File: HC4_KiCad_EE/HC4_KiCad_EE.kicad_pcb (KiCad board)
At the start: 2 copper layers, 150.4 x 175 mm, 168 parts, among them IC1 RAM, IC10 74HC4002, IC11 74HC161, IC12 74HC377, IC13 74HC161, IC14 74HC161, IC15 74HC161, IC16 74HC257, IC17 74HC257, IC18 74HC32, IC19 74HC74, IC2 ROM, IC20 74HC00, IC21 74HC4053, IC22 74HC04, IC23 74HC151, IC24 74HC14, IC3 74HC153, IC4 74HC153, IC5 74HC153, IC6 74HC153, IC7 74HC283, IC8 74HC257, IC9 74HC244, J1 Power, J2 CE, J3 Expantion_Connector, SW1 SW_SPDT, SW2 Bus_Open, SW3 SW_Push, SW4 SW_Push, SW5 SW_SPDT

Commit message: チップ集合抵抗に変更、基板作成開始
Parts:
- removed CP19, CP20, CP21, CP22, CP23, CP24: 0.1u, Capacitor_THT:C_Disc_D3.0mm_W1.6mm_P2.50mm
- removed D10, D11, D12, D13, D14, D15, D16, D17, D18, D19, D2, D20, D21, D22, D23, D24, D25, D26, D27, D28, D29, D3, D30, D31, D32, D33, D34, D35, D36, D37, D38, D39, D4, D40, D41, D5, D6, D7, D8, D9: D, Library:DO-35_horizontal_anodeup_Smallhole
- removed G***: LOGO, LOGO
- removed IC16, IC17: 74HC257, Package_DIP:DIP-16_W7.62mm_Socket
- removed IC18: 74HC32, Package_DIP:DIP-14_W7.62mm_Socket
- removed IC19: 74HC74, Package_DIP:DIP-14_W7.62mm_Socket
- removed IC20: 74HC00, Package_DIP:DIP-14_W7.62mm_Socket
- removed IC21: 74HC4053, Package_DIP:DIP-16_W7.62mm_Socket
- removed IC22: 74HC04, Package_DIP:DIP-14_W7.62mm_Socket
- removed IC23: 74HC151, Package_DIP:DIP-16_W7.62mm_Socket
- removed IC24: 74HC14, Package_DIP:DIP-14_W7.62mm_Socket
- removed JP1: Jumper, Connector_PinHeader_2.54mm:PinHeader_1x03_P2.54mm_Vertical
- removed R10: 100k, Resistor_THT:R_Axial_DIN0207_L6.3mm_D2.5mm_P7.62mm_Horizontal
- removed R11: Socket, Resistor_THT:R_Axial_DIN0207_L6.3mm_D2.5mm_P7.62mm_Horizontal
- removed R12, R15: 100, Resistor_THT:R_Axial_DIN0207_L6.3mm_D2.5mm_P7.62mm_Horizontal
- removed R13, R14: 1k, Resistor_THT:R_Axial_DIN0207_L6.3mm_D2.5mm_P7.62mm_Horizontal
- added C5: 10u, Capacitor_THT:C_Radial_D5.0mm_H5.0mm_P2.00mm, F.Cu at (190.7, 110.7)
- added H1: MountingHole, MountingHole:MountingHole_3.2mm_M3, F.Cu at (141.5, 62.5)
- added H2: MountingHole, MountingHole:MountingHole_3.2mm_M3, F.Cu at (48.5, 62.5)
- added H3: MountingHole, MountingHole:MountingHole_3.2mm_M3, F.Cu at (48.5, 151.5)
- added H4: MountingHole, MountingHole:MountingHole_3.2mm_M3, F.Cu at (141.5, 151.5)
- added J4: AVR-UPDI-6, Connector_PinHeader_2.54mm:PinHeader_2x03_P2.54mm_Vertical, F.Cu at (260.4, 90.8)
- added LD42: Chip, LED_SMD:LED_0603_1608Metric, F.Cu at (254.1, 66.3)
- added LD43: Chip, LED_SMD:LED_0603_1608Metric, F.Cu at (254.1, 68.9)
- added LD44: CLK, LED_THT:LED_D5.0mm, F.Cu at (180.3, 107.1)
- added LD45: RESET, LED_THT:LED_D5.0mm, F.Cu at (180.3, 114.5)
- added LD46: Chip, LED_SMD:LED_0603_1608Metric, F.Cu at (268.1, 69.5)
- added LD47: Chip, LED_SMD:LED_0603_1608Metric, F.Cu at (268.1, 72.1)
- added LD48: Chip, LED_SMD:LED_0603_1608Metric, F.Cu at (268.1, 74.7)
- added LD49: Chip, LED_SMD:LED_0603_1608Metric, F.Cu at (268.1, 77.2)
- added RN10: 1k, Resistor_SMD:R_Array_Convex_4x0603, F.Cu at (255.0, 116.8)
- added RN11: 1k, Resistor_SMD:R_Array_Convex_4x0603, F.Cu at (246.1, 57.4)
- added RN12: 1k, Resistor_SMD:R_Array_Convex_4x0603, F.Cu at (250.2, 57.4)
- added RN13: 1k, Resistor_SMD:R_Array_Convex_4x0603, F.Cu at (254.4, 57.4)
- added RN14: 1k, Resistor_SMD:R_Array_Convex_4x0603, F.Cu at (197.0, 109.8)
- added RN15: 1k, Resistor_SMD:R_Array_Convex_4x0603, F.Cu at (272.1, 70.6)
- added RN9: 1k, Resistor_SMD:R_Array_Convex_4x0603, F.Cu at (250.8, 116.8)
- added U1: ATmega4809-A, Package_QFP:TQFP-48_7x7mm_P0.5mm, F.Cu at (67.9, 146.7)
- added U2: CH340E, Package_SO:MSOP-10_3x3mm_P0.5mm, F.Cu at (57.8, 141.6)
- C2: value 10u -> 0.1u; footprint Capacitor_THT:CP_Radial_D5.0mm_P2.50mm -> Capacitor_SMD:C_0603_1608Metric
- C4: value 10u(Socket) -> 10u; footprint Capacitor_THT:C_Radial_D5.0mm_H5.0mm_P2.00mm -> Capacitor_THT:CP_Radial_D5.0mm_P2.50mm
- CP1, CP10, CP11, CP12, CP13, CP14, CP15, CP16, CP17, CP18, CP2, CP3, CP4, CP5, CP6, CP7, CP8, CP9: footprint Capacitor_THT:C_Disc_D3.0mm_W1.6mm_P2.50mm -> Capacitor_SMD:C_0603_1608Metric
- D1: value 5.6V -> C-551SRD; footprint Diode_THT:D_DO-34_SOD68_P7.62mm_Horizontal -> Display_7Segment:D1X8K
- F1: value Polyfuse -> 500mA
- IC1: value RAM -> 74HC86; footprint Package_DIP:DIP-28_W15.24mm -> Package_SO:SO-14_5.3x10.2mm_P1.27mm
- IC10: value 74HC4002 -> 74HC161; footprint Package_DIP:DIP-14_W7.62mm_Socket -> Package_SO:SO-16_5.3x10.2mm_P1.27mm
- IC11: value 74HC161 -> 74HC02; footprint Package_DIP:DIP-16_W7.62mm_Socket -> Package_SO:SO-14_5.3x10.2mm_P1.27mm
- IC12: value 74HC377 -> 74HC00; footprint Package_DIP:DIP-20_W7.62mm_Socket -> Package_SO:SO-14_5.3x10.2mm_P1.27mm
- IC13: value 74HC161 -> 74HC4053; footprint Package_DIP:DIP-16_W7.62mm_Socket -> Package_SO:SO-16_5.3x10.2mm_P1.27mm
- IC14: value 74HC161 -> 74HC74; footprint Package_DIP:DIP-16_W7.62mm_Socket -> Package_SO:SO-14_5.3x10.2mm_P1.27mm
- IC15: value 74HC161 -> 74HC14; footprint Package_DIP:DIP-16_W7.62mm_Socket -> Package_SO:SO-14_5.3x10.2mm_P1.27mm
- IC2: value ROM -> 74HC283; footprint Package_DIP:DIP-28_W15.24mm -> Package_SO:SO-16_5.3x10.2mm_P1.27mm
- IC3, IC4: value 74HC153 -> 74HC253; footprint Package_DIP:DIP-16_W7.62mm_Socket -> Package_SO:SO-16_5.3x10.2mm_P1.27mm
- IC5: value 74HC153 -> 74HC244; footprint Package_DIP:DIP-16_W7.62mm_Socket -> Package_SO:TSSOP-20_4.4x6.5mm_P0.65mm
- IC6: value 74HC153 -> 74HC377; footprint Package_DIP:DIP-16_W7.62mm_Socket -> Package_SO:TSSOP-20_4.4x6.5mm_P0.65mm
- IC7: value 74HC283 -> 4511; footprint Package_DIP:DIP-16_W7.62mm_Socket -> Package_SO:SO-16_5.3x10.2mm_P1.27mm
- IC8: value 74HC257 -> 74HC377; footprint Package_DIP:DIP-16_W7.62mm_Socket -> Package_SO:TSSOP-20_4.4x6.5mm_P0.65mm
- IC9: value 74HC244 -> 74HC161; footprint Package_DIP:DIP-20_W7.62mm_Socket -> Package_SO:SO-16_5.3x10.2mm_P1.27mm
- J1: value Power -> USB_B_Mini; footprint Connector_BarrelJack:BarrelJack_GCT_DCJ200-10-A_Horizontal -> Connector_USB:USB_Mini-B_Wuerth_65100516121_Horizontal
- J2: value CE -> Port_IN; footprint Connector_PinSocket_2.54mm:PinSocket_1x01_P2.54mm_Vertical -> Connector_PinHeader_2.54mm:PinHeader_1x04_P2.54mm_Vertical
- J3: value Expantion_Connector -> Port_A; footprint Connector_PinHeader_2.54mm:PinHeader_2x20_P2.54mm_Vertical -> Connector_PinHeader_2.54mm:PinHeader_1x04_P2.54mm_Vertical
- LD2: value LED -> Carry
- LD31: value LED -> ACT; footprint LED_THT:LED_Rectangular_W5.0mm_H2.0mm -> LED_SMD:LED_0603_1608Metric
- LD32, LD33, LD34, LD35, LD36, LD37, LD38, LD39: value LED -> Chip; footprint LED_THT:LED_Rectangular_W5.0mm_H2.0mm -> LED_SMD:LED_0603_1608Metric
- LD40, LD41: value D -> Chip; footprint LED_THT:LED_D5.0mm -> LED_SMD:LED_0603_1608Metric
- R1, R2, R3, R4: footprint Resistor_THT:R_Axial_DIN0207_L6.3mm_D2.5mm_P7.62mm_Horizontal -> Resistor_SMD:R_0603_1608Metric
- R5: value 10k -> 100k; footprint Resistor_THT:R_Axial_DIN0207_L6.3mm_D2.5mm_P7.62mm_Horizontal -> Resistor_SMD:R_0603_1608Metric
- R6: value 10k -> 33k; footprint Resistor_THT:R_Axial_DIN0207_L6.3mm_D2.5mm_P7.62mm_Horizontal -> Resistor_SMD:R_0603_1608Metric
- R7: value 1k -> 3.3k; footprint Resistor_THT:R_Axial_DIN0207_L6.3mm_D2.5mm_P7.62mm_Horizontal -> Resistor_SMD:R_0603_1608Metric
- R8: value 1k -> 100; footprint Resistor_THT:R_Axial_DIN0207_L6.3mm_D2.5mm_P7.62mm_Horizontal -> Resistor_SMD:R_0603_1608Metric
- R9: value 10k -> 100; footprint Resistor_THT:R_Axial_DIN0207_L6.3mm_D2.5mm_P7.62mm_Horizontal -> Resistor_SMD:R_0603_1608Metric
- RN1, RN2, RN5: footprint Resistor_THT:R_Array_SIP5 -> Resistor_SMD:R_Array_Convex_4x0603
- RN3: value R_Network04_Split -> 1k; footprint Resistor_THT:R_Array_SIP5 -> Resistor_SMD:R_Array_Convex_4x0603
- RN4: value R_Network08_Split -> 1k; footprint Resistor_THT:R_Array_SIP9 -> Resistor_SMD:R_Array_Convex_4x0603
- RN6, RN7: footprint Resistor_THT:R_Array_SIP9 -> Resistor_SMD:R_Array_Convex_4x0603
- RN8: value 10k -> 1k; footprint Resistor_THT:R_Array_SIP9 -> Resistor_SMD:R_Array_Convex_4x0603
- SW1: value SW_SPDT -> SW_DIP_x04; footprint Button_Switch_THT:SW_Slide-03_Wuerth-WS-SLTV_10x2.5x6.4_P2.54mm -> Button_Switch_THT:SW_DIP_SPSTx04_Slide_9.78x12.34mm_W7.62mm_P2.54mm
- SW2: value Bus_Open -> SW_Push; footprint Button_Switch_THT:SW_Slide-03_Wuerth-WS-SLTV_10x2.5x6.4_P2.54mm -> Button_Switch_THT:SW_PUSH_6mm
- SW4: value SW_Push -> FreqSel; footprint Button_Switch_THT:SW_PUSH_6mm -> Button_Switch_THT:SW_Slide-03_Wuerth-WS-SLTV_10x2.5x6.4_P2.54mm
- moved F1 227.7 mm to (231.9, 56.8)
- moved LD41 224.6 mm to (254.1, 63.7), turned to 0 degrees
- moved LD40 222.7 mm to (254.1, 61.1), turned to 0 degrees
- moved RN7 218.0 mm to (229.5, 119.5)
- moved C1 217.7 mm to (237.5, 70.4), turned to 0 degrees
- moved LD32 214.8 mm to (246.0, 61.1), turned to 0 degrees
- moved LD33 212.7 mm to (246.0, 63.7), turned to 0 degrees
- moved LD34 210.6 mm to (246.0, 66.3), turned to 0 degrees
- moved CP17 210.2 mm to (268.9, 63.9), turned to 0 degrees
- moved LD36 208.8 mm to (250.1, 61.1), turned to 0 degrees
- moved LD35 208.5 mm to (246.0, 68.9), turned to 0 degrees
- moved CP16 208.3 mm to (268.9, 61.3), turned to 0 degrees
- moved C2 207.5 mm to (256.1, 78.4), turned to 0 degrees
- moved LD37 206.6 mm to (250.1, 63.7), turned to 0 degrees
- moved LD38 204.5 mm to (250.1, 66.3), turned to 0 degrees
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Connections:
- C2 pad 1: Net-(C2-Pad1) -> GND
- C2 pad 2: GND -> Net-(U2-V3)
- C4 pad 2: Net-(SW5-A) -> GND
- D1 pad 1: VCC -> Net-(D1-E)
- D1 pad 2: GND -> Net-(D1-D)
- IC1 pad 1: VCC -> /ALU/ALU_in_A0
- IC1 pad 10: /Address BUS/RAM_A0 -> /ALU/ALU_in_B2
- IC1 pad 11: /Data BUS/Stack0 -> /ALU/XOR3
- IC1 pad 12: /Data BUS/Stack1 -> /ALU/ALU_in_A3
- IC1 pad 13: /Data BUS/Stack2 -> /ALU/ALU_in_B3
- IC1 pad 14: GND -> VCC
- IC1 pad 2: VCC -> /ALU/ALU_in_B0
- IC1 pad 3: /Address BUS/RAM_A7 -> /ALU/XOR0
- IC1 pad 4: /Address BUS/RAM_A6 -> /ALU/ALU_in_A1
- IC1 pad 5: /Address BUS/RAM_A5 -> /ALU/ALU_in_B1
- IC1 pad 6: /Address BUS/RAM_A4 -> /ALU/XOR1
- IC1 pad 7: /Address BUS/RAM_A3 -> GND
- IC1 pad 8: /Address BUS/RAM_A2 -> /ALU/XOR2
- IC1 pad 9: /Address BUS/RAM_A1 -> /ALU/ALU_in_A2
- IC10 pad 1: /ALU/I1a -> ~{RESET}
- IC10 pad 10: /Data BUS/Stack2 -> VCC
- IC10 pad 11: /Data BUS/Stack1 -> /Program Counter/PC_3
- IC10 pad 12: /Data BUS/Stack0 -> /Program Counter/PC_2
- IC10 pad 13: /Data BUS/BUS_Zero -> /Program Counter/PC_1
- IC10 pad 14: VCC -> /Program Counter/PC_0
- IC10 pad 2: Net-(D18-K) -> CLK
- IC10 pad 3: Net-(D18-K) -> /ALU/ALU_in_A0
- IC10 pad 4: Net-(D22-K) -> /ALU/ALU_in_A1
- IC10 pad 5: Net-(D22-K) -> /ALU/ALU_in_A2
- IC10 pad 6: (no net) -> /ALU/ALU_in_A3
- IC10 pad 7: GND -> VCC
- IC10 pad 8: (no net) -> GND
- IC10 pad 9: /Data BUS/Stack3 -> /Instruction Decoder/~{JMP}
- IC11 pad 1: ~{RESET} -> /Instruction Decoder/READ
- IC11 pad 10: GND -> /Instruction Decoder/Carry_EN
- IC11 pad 11: /ALU/ALU_in_A3 -> VCC
- IC11 pad 12: /ALU/ALU_in_A2 -> VCC
- IC11 pad 13: /ALU/ALU_in_A1 -> unconnected-(IC11-Pad13)
- IC11 pad 14: /ALU/ALU_in_A0 -> VCC
- IC11 pad 2: CLK -> /ALU/Instruction_6
- IC11 pad 3: /Data BUS/Stack0 -> /ALU/Instruction_5
- IC11 pad 4: /Data BUS/Stack1 -> unconnected-(IC11-Pad4)
- IC11 pad 5: /Data BUS/Stack2 -> VCC
- IC11 pad 6: /Data BUS/Stack3 -> VCC
- IC11 pad 8: GND -> /ALU/Instruction_7
- IC11 pad 9: /Instruction Decoder/~{STACK_LE} -> /ALU/Instruction_6
- IC12 pad 1: /Instruction Decoder/~{STACK_LE} -> /Instruction Decoder/READ
- IC12 pad 10: GND -> /ALU/Instruction_6
- IC12 pad 11: CLK -> /Instruction Decoder/~{STACK_LE}
- IC12 pad 12: /Data BUS/Level_C0 -> /Instruction Decoder/~{Is_JP}
- IC12 pad 13: /ALU/ALU_in_B3 -> /ALU/Instruction_7
- IC12 pad 14: /ALU/ALU_in_B2 -> VCC
- IC12 pad 2: /ALU/ALU_in_B0 -> CLK2
- IC12 pad 3: /ALU/ALU_in_A0 -> /Instruction Decoder/~{RAM_RD}
- IC12 pad 4: /ALU/ALU_in_A1 -> /ALU/Instruction_7
- IC12 pad 5: /ALU/ALU_in_B1 -> CLK2
- IC12 pad 6: /ALU/ALU_in_B2 -> /Instruction Decoder/~{RAM_WR}
- IC12 pad 7: /ALU/ALU_in_A2 -> GND
- IC12 pad 8: /ALU/ALU_in_A3 -> /Instruction Decoder/~{Is_JP}
- IC12 pad 9: /ALU/ALU_in_B3 -> /ALU/Instruction_7
- IC13 pad 1: ~{RESET} -> /Instruction Decoder/Carry_Flg
- IC13 pad 10: Net-(IC13-ENT) -> /ALU/Instruction_1
- IC13 pad 11: /Program Counter/PC_8 -> /Instruction Decoder/Carry_EN
- IC13 pad 12: /Program Counter/PC_9 -> /Instruction Decoder/Carry_Flg
- IC13 pad 13: /Program Counter/PC_10 -> /ALU/Carry_OUT
- IC13 pad 14: /Program Counter/PC_11 -> Net-(IC13-X)
- IC13 pad 15: unconnected-(IC13-CO-Pad15) -> Net-(IC13-Y)
- IC13 pad 2: CLK -> /ALU/Instruction_0
- IC13 pad 3: /Data BUS/Level_C3 -> VCC
- IC13 pad 4: /Data BUS/Level_C2 -> /Instruction Decoder/~{JMP}
- IC13 pad 5: /Data BUS/Level_C1 -> Net-(IC13-Y)
- IC13 pad 6: /Data BUS/Level_C0 -> GND
- IC13 pad 7: VCC -> GND
- IC13 pad 9: /Instruction Decoder/~{JMP} -> /Instruction Decoder/~{Is_JP}
- IC14 pad 10: Net-(IC14-ENT) -> VCC
- IC14 pad 11: /Program Counter/PC_4 -> VCC
- IC14 pad 12: /Program Counter/PC_5 -> VCC
- IC14 pad 13: /Program Counter/PC_6 -> VCC
- IC14 pad 14: /Program Counter/PC_7 -> VCC
- IC14 pad 2: CLK -> Net-(IC13-X)
- IC14 pad 3: /ALU/ALU_in_B3 -> CLK
- IC14 pad 4: /ALU/ALU_in_B2 -> VCC
- IC14 pad 5: /ALU/ALU_in_B1 -> /Instruction Decoder/Carry_Flg
- IC14 pad 6: /ALU/ALU_in_B0 -> unconnected-(IC14A-~{Q}-Pad6)
- IC14 pad 7: VCC -> GND
- IC14 pad 8: GND -> unconnected-(IC14B-~{Q}-Pad8)
- IC14 pad 9: /Instruction Decoder/~{JMP} -> unconnected-(IC14B-Q-Pad9)
- IC15 pad 1: ~{RESET} -> Net-(C5-Pad1)
- IC15 pad 10: VCC -> Net-(SW5-C)
- IC15 pad 11: /Program Counter/PC_0 -> Net-(C3-Pad1)
- IC15 pad 12: /Program Counter/PC_1 -> Net-(IC15-Pad12)
- IC15 pad 13: /Program Counter/PC_2 -> CLK2
- IC15 pad 14: /Program Counter/PC_3 -> VCC
- IC15 pad 2: CLK -> Net-(SW4-B)
- IC15 pad 3: /ALU/ALU_in_A3 -> Net-(SW4-B)
- IC15 pad 4: /ALU/ALU_in_A2 -> Net-(SW5-A)
- IC15 pad 5: /ALU/ALU_in_A1 -> Net-(C4-Pad1)
- IC15 pad 6: /ALU/ALU_in_A0 -> Net-(IC15-Pad6)
- IC15 pad 7: VCC -> GND
- IC15 pad 8: GND -> ~{RESET}
- IC15 pad 9: /Instruction Decoder/~{JMP} -> Net-(IC15-Pad6)
- IC2 pad 1: VCC -> /ALU/ADDER1
- IC2 pad 10: /Program Counter/PC_0 -> /ALU/ADDER3
- IC2 pad 11: /Address BUS/Instruction_0 -> /ALU/ALU_in_B3
- IC2 pad 12: /Address BUS/Instruction_1 -> /ALU/ALU_in_A3
- IC2 pad 13: /Address BUS/Instruction_2 -> /ALU/ADDER2
- IC2 pad 14: GND -> /ALU/ALU_in_A2
- IC2 pad 15: /Address BUS/Instruction_3 -> /ALU/ALU_in_B2
- IC2 pad 16: /Address BUS/Instruction_4 -> VCC
- IC2 pad 2: VCC -> /ALU/ALU_in_B1
- IC2 pad 3: /Program Counter/PC_7 -> /ALU/ALU_in_A1
- IC2 pad 4: /Program Counter/PC_6 -> /ALU/ADDER0
- IC2 pad 5: /Program Counter/PC_5 -> /ALU/ALU_in_A0
- IC2 pad 6: /Program Counter/PC_4 -> /ALU/ALU_in_B0
- IC2 pad 7: /Program Counter/PC_3 -> GND
- IC2 pad 8: /Program Counter/PC_2 -> GND
- IC2 pad 9: /Program Counter/PC_1 -> /ALU/Carry_OUT
- IC3 pad 1: GND -> /Instruction Decoder/READ
- IC3 pad 10: GND -> /ALU/Instruction_1
- IC3 pad 11: VCC -> /ALU/ADDER1
- IC3 pad 12: GND -> /ALU/XOR1
- IC3 pad 13: VCC -> /ALU/ALU_in_A1
- IC3 pad 14: /ALU/ALU_in_A3 -> /ALU/Instruction_4
- IC3 pad 15: /Instruction Decoder/ALU_~{Eb} -> /Instruction Decoder/READ
- IC3 pad 2: /ALU/ALU_in_B3 -> /ALU/Instruction_6
- IC3 pad 3: /ALU/I3a -> /ALU/ALU_in_A0
- IC3 pad 4: /ALU/I2a -> /ALU/XOR0
- IC3 pad 5: /ALU/I1a -> /ALU/ADDER0
- IC3 pad 6: /ALU/I0a -> /ALU/Instruction_0
- IC3 pad 7: /ALU/Internal_A3 -> /ALU/ALU_OUT0
- IC3 pad 9: /ALU/Internal_B3 -> /ALU/ALU_OUT1
- IC4 pad 1: GND -> /Instruction Decoder/READ
- IC4 pad 10: GND -> /ALU/Instruction_3
- IC4 pad 11: VCC -> /ALU/ADDER3
- IC4 pad 12: GND -> /ALU/XOR3
- IC4 pad 13: VCC -> /ALU/ALU_in_A3
- IC4 pad 14: /ALU/ALU_in_A2 -> /ALU/Instruction_4
- IC4 pad 15: /Instruction Decoder/ALU_~{Eb} -> /Instruction Decoder/READ
- IC4 pad 2: /ALU/ALU_in_B2 -> /ALU/Instruction_6
- IC4 pad 3: /ALU/I3a -> /ALU/ALU_in_A2
- IC4 pad 4: /ALU/I2a -> /ALU/XOR2
- IC4 pad 5: /ALU/I1a -> /ALU/ADDER2
- IC4 pad 6: /ALU/I0a -> /ALU/Instruction_2
- IC4 pad 7: /ALU/Internal_A2 -> /ALU/ALU_OUT2
- IC4 pad 9: /ALU/Internal_B2 -> /ALU/ALU_OUT3
- IC5 pad 1: GND -> /Data BUS/~{IN_PORT_OE}
- IC5 pad 11: VCC -> /ALU/ALU_OUT3
- IC5 pad 12: GND -> /ALU/ALU_OUT3
- IC5 pad 13: VCC -> /ALU/ALU_OUT2
- IC5 pad 14: /ALU/ALU_in_A1 -> /ALU/ALU_OUT2
- IC5 pad 15: /Instruction Decoder/ALU_~{Eb} -> /ALU/ALU_OUT1
- IC5 pad 16: VCC -> /ALU/ALU_OUT1
- IC5 pad 2: /ALU/ALU_in_B1 -> Net-(IC5-1A0)
- IC5 pad 3: /ALU/I3a -> Net-(IC5-2Y0)
- IC5 pad 4: /ALU/I2a -> Net-(IC5-1A1)
- IC5 pad 5: /ALU/I1a -> Net-(IC5-2Y1)
- IC5 pad 6: /ALU/I0a -> Net-(IC5-1A2)
- IC5 pad 7: /ALU/Internal_A1 -> Net-(IC5-2Y2)
- IC5 pad 8: GND -> Net-(IC5-1A3)
- IC5 pad 9: /ALU/Internal_B1 -> Net-(IC5-2Y3)
- IC6 pad 11: VCC -> /Data BUS/~{PORTA_OUT_OE}
- IC6 pad 12: GND -> Net-(IC6-Q4)
- IC6 pad 13: VCC -> /ALU/ALU_OUT0
- IC6 pad 14: /ALU/ALU_in_A0 -> /ALU/ALU_OUT1
- IC6 pad 15: /Instruction Decoder/ALU_~{Eb} -> Net-(IC6-Q5)
- IC6 pad 16: VCC -> Net-(IC6-Q6)
- IC6 pad 2: /ALU/ALU_in_B0 -> Net-(IC6-Q0)
- IC6 pad 3: /ALU/I3a -> /ALU/ALU_OUT0
- IC6 pad 4: /ALU/I2a -> /ALU/ALU_OUT1
- IC6 pad 5: /ALU/I1a -> Net-(IC6-Q1)
- IC6 pad 6: /ALU/I0a -> Net-(IC6-Q2)
- IC6 pad 7: /ALU/Internal_A0 -> /ALU/ALU_OUT2
- IC6 pad 8: GND -> /ALU/ALU_OUT3
- IC6 pad 9: /ALU/Internal_B0 -> Net-(IC6-Q3)
- IC7 pad 10: /ALU/ALU_OUT3 -> Net-(IC7-Qd)
- IC7 pad 11: /ALU/Internal_B3 -> Net-(IC7-Qc)
- IC7 pad 12: /ALU/Internal_A3 -> Net-(IC7-Qb)
- IC7 pad 13: /ALU/ALU_OUT2 -> Net-(IC7-Qa)
- IC7 pad 14: /ALU/Internal_A2 -> Net-(IC7-Qg)
- IC7 pad 15: /ALU/Internal_B2 -> Net-(IC7-Qf)
- IC7 pad 2: /ALU/Internal_B1 -> /ALU/ALU_OUT2
- IC7 pad 3: /ALU/Internal_A1 -> VCC
- IC7 pad 4: /ALU/ALU_OUT0 -> VCC
- IC7 pad 5: /ALU/Internal_A0 -> /Data BUS/~{PORTB_OUT_OE}
- IC7 pad 6: /ALU/Internal_B0 -> /ALU/ALU_OUT3
- IC7 pad 7: /Instruction Decoder/Carry_Flg -> /ALU/ALU_OUT0
- IC7 pad 9: /ALU/Carry_OUT -> Net-(IC7-Qe)
- IC8 pad 1: /Data BUS/Level_C_OE -> /Instruction Decoder/~{STACK_LE}
- IC8 pad 10: /Data BUS/Level_C3 -> GND
- IC8 pad 11: /ALU/ALU_OUT3 -> CLK
- IC8 pad 12: /Data BUS/Stack2 -> /ALU/ALU_in_B3
- IC8 pad 13: /Data BUS/Level_C2 -> /ALU/ALU_in_A0
- IC8 pad 14: /ALU/ALU_OUT2 -> /ALU/ALU_in_A1
- IC8 pad 15: /Address BUS/Instruction_7 -> /ALU/ALU_in_B2
- IC8 pad 16: VCC -> /ALU/ALU_in_B1
- IC8 pad 2: /ALU/ALU_OUT0 -> /ALU/ALU_in_A0
- IC8 pad 3: /Data BUS/Level_C0 -> /ALU/ALU_OUT0
- IC8 pad 4: /Data BUS/Stack0 -> /ALU/ALU_OUT1
- IC8 pad 5: /ALU/ALU_OUT1 -> /ALU/ALU_in_A1
- IC8 pad 6: /Data BUS/Level_C1 -> /ALU/ALU_in_A2
- IC8 pad 7: /Data BUS/Stack1 -> /ALU/ALU_OUT2
- IC8 pad 8: GND -> /ALU/ALU_OUT3
- IC8 pad 9: /Data BUS/Stack3 -> /ALU/ALU_in_A3
- IC9 pad 1: /Data BUS/~{Immediate_OE} -> ~{RESET}
- IC9 pad 10: GND -> Net-(IC10-CO)
- IC9 pad 11: /Data BUS/Stack3 -> /Program Counter/PC_7
- IC9 pad 12: /Data BUS/Stack3 -> /Program Counter/PC_6
- IC9 pad 13: /Data BUS/Stack2 -> /Program Counter/PC_5
- IC9 pad 14: /Data BUS/Stack2 -> /Program Counter/PC_4
- IC9 pad 15: /Data BUS/Stack1 -> unconnected-(IC9-CO-Pad15)
- IC9 pad 16: /Data BUS/Stack1 -> VCC
- IC9 pad 2: /Address BUS/Instruction_0 -> CLK
- IC9 pad 3: Net-(IC9-2Y0) -> /ALU/ALU_in_B0
- IC9 pad 4: /Address BUS/Instruction_1 -> /ALU/ALU_in_B1
- IC9 pad 5: Net-(IC9-2Y1) -> /ALU/ALU_in_B2
- IC9 pad 6: /Address BUS/Instruction_2 -> /ALU/ALU_in_B3
- IC9 pad 7: Net-(IC9-2Y2) -> VCC
- IC9 pad 8: /Address BUS/Instruction_3 -> GND
- IC9 pad 9: Net-(IC9-2Y3) -> /Instruction Decoder/~{JMP}
- J1 pad 2: GND -> D-
- J1 pad 3: (no net) -> D+
- J2 pad 1: Net-(J2-Pin_1) -> Net-(IC5-1A0)
- J3 pad 1: /Data BUS/~{RD} -> Net-(IC6-Q0)
- J3 pad 2: /Data BUS/~{WR} -> Net-(IC6-Q1)
- J3 pad 3: /Data BUS/Stack0 -> Net-(IC6-Q2)
- J3 pad 4: /Data BUS/Stack1 -> Net-(IC6-Q3)
- LD10 pad 2: /Data BUS/Level_C1 -> Net-(IC6-Q5)
- LD11 pad 2: /Data BUS/Level_C0 -> /ALU/Instruction_2
- LD12 pad 2: /ALU/ALU_in_B3 -> Net-(IC6-Q4)
- LD13 pad 2: /ALU/ALU_in_B2 -> /ALU/Instruction_1
- LD14 pad 2: /ALU/ALU_in_B1 -> /ALU/Instruction_0
- LD15 pad 2: /ALU/ALU_in_B0 -> /ALU/ALU_in_A0
- LD16 pad 2: /ALU/ALU_in_A3 -> /ALU/ALU_in_A1
- LD18 pad 2: /ALU/ALU_in_A1 -> /ALU/ALU_in_A3
- LD19 pad 2: /ALU/ALU_in_A0 -> /ALU/ALU_in_B0
- LD2 pad 2: /Instruction Decoder/Zero_Flg -> /Instruction Decoder/Carry_Flg
- LD20 pad 2: /Program Counter/PC_11 -> /ALU/ALU_in_B1
- LD21 pad 2: /Program Counter/PC_7 -> /ALU/ALU_in_B2
- LD22 pad 2: /Program Counter/PC_3 -> /ALU/ALU_in_B3
- LD23 pad 2: /Program Counter/PC_10 -> /Program Counter/PC_7
- LD24 pad 2: /Program Counter/PC_6 -> /Program Counter/PC_3
- LD25 pad 2: /Program Counter/PC_2 -> /Program Counter/PC_6
- LD26 pad 2: /Program Counter/PC_9 -> /Program Counter/PC_2
- LD29 pad 2: /Program Counter/PC_8 -> /Program Counter/PC_4
- LD3 pad 2: /Instruction Decoder/Carry_Flg -> Net-(IC5-2Y3)
- LD30 pad 2: /Program Counter/PC_4 -> /Program Counter/PC_0
- LD31 pad 2: /Program Counter/PC_0 -> Net-(U2-TNOW)
- LD32 pad 2: /Address BUS/RAM_A7 -> /Instruction Decoder/~{Is_JP}
- LD33 pad 2: /Address BUS/RAM_A6 -> /Instruction Decoder/Carry_EN
- LD34 pad 2: /Address BUS/RAM_A5 -> /Instruction Decoder/READ
- LD35 pad 2: /Address BUS/RAM_A4 -> /Instruction Decoder/~{JMP}
- LD36 pad 2: /Address BUS/RAM_A3 -> /Instruction Decoder/~{RAM_WR}
- LD37 pad 2: /Address BUS/RAM_A2 -> /Instruction Decoder/~{RAM_RD}
- LD38 pad 2: /Address BUS/RAM_A1 -> /Instruction Decoder/~{STACK_LE}
- LD39 pad 2: /Address BUS/RAM_A0 -> /ALU/Carry_OUT
- LD4 pad 2: Net-(IC9-2Y3) -> Net-(IC5-2Y2)
- LD40 pad 1: CLK -> Net-(LD40-K)
- LD40 pad 2: Net-(LD40-Pad2) -> /ALU/Instruction_7
- LD41 pad 1: ~{RESET} -> Net-(LD41-K)
- LD41 pad 2: Net-(LD41-Pad2) -> /ALU/Instruction_6
- LD5 pad 2: Net-(IC9-2Y2) -> Net-(IC5-2Y1)
- LD6 pad 2: Net-(IC9-2Y1) -> Net-(IC5-2Y0)
- LD7 pad 2: Net-(IC9-2Y0) -> Net-(IC6-Q7)
- LD8 pad 2: /Data BUS/Level_C3 -> Net-(IC6-Q6)
- LD9 pad 2: /Data BUS/Level_C2 -> /ALU/Instruction_3
- R3 pad 1: Net-(LD3-K) -> Net-(LD31-K)
- R4 pad 1: Net-(IC16-OE) -> Net-(RN14A-R1.1)
- R4 pad 2: GND -> Net-(C3-Pad1)
- R5 pad 1: VCC -> Net-(RN14B-R2.1)
- R5 pad 2: /Instruction Decoder/READ -> Net-(C4-Pad1)
- R6 pad 1: VCC -> Net-(C5-Pad1)
- R6 pad 2: /Data BUS/Level_C_OE -> Net-(SW4-A)
- R7 pad 1: VCC -> Net-(C5-Pad1)
- R7 pad 2: Net-(R7-Pad2) -> Net-(SW4-C)
- R8 pad 1: VCC -> Net-(SW5-B)
- R8 pad 2: Net-(R10-Pad1) -> CLK2
- R9 pad 1: Net-(R7-Pad2) -> Net-(IC15-Pad12)
- R9 pad 2: Net-(C2-Pad1) -> CLK
- RN1 pad 1: VCC -> GND
- RN1 pad 2: Net-(IC1-Q7) -> GND
- RN1 pad 3: Net-(IC1-Q6) -> GND
- RN1 pad 4: Net-(IC1-Q5) -> GND
- RN1 pad 5: Net-(IC1-Q4) -> Net-(IC5-1A0)
- RN2 pad 2: Net-(LD4-K) -> GND
- RN2 pad 3: Net-(LD5-K) -> GND
- RN2 pad 4: Net-(LD6-K) -> GND
- RN2 pad 5: Net-(LD7-K) -> Net-(LD6-K)
- RN3 pad 2: Net-(LD11-K) -> GND
- RN3 pad 3: Net-(LD10-K) -> GND
- RN3 pad 4: Net-(LD9-K) -> GND
- RN3 pad 5: Net-(LD8-K) -> Net-(LD7-K)
- RN4 pad 2: Net-(LD19-K) -> GND
- RN4 pad 3: Net-(LD18-K) -> GND
- RN4 pad 4: Net-(LD17-K) -> GND
- RN4 pad 5: Net-(LD16-K) -> Net-(LD14-K)
- RN4 pad 6: Net-(LD15-K) -> Net-(LD13-K)
- RN4 pad 7: Net-(LD14-K) -> Net-(LD11-K)
- RN4 pad 8: Net-(LD13-K) -> Net-(LD9-K)
- RN5 pad 1: GND -> Net-(IC7-Qa)
- RN5 pad 2: Net-(LD20-K) -> Net-(IC7-Qb)
- RN5 pad 3: Net-(LD23-K) -> Net-(IC7-Qc)
- RN5 pad 4: Net-(LD26-K) -> Net-(IC7-Qd)
- RN5 pad 5: Net-(LD29-K) -> Net-(D1-D)
- RN6 pad 1: GND -> Net-(IC7-Qe)
- RN6 pad 2: Net-(LD31-K) -> Net-(IC7-Qf)
- RN6 pad 3: Net-(LD28-K) -> Net-(IC7-Qg)
- RN6 pad 4: Net-(LD25-K) -> /Data BUS/~{PORTB_OUT_OE}
- RN6 pad 5: Net-(LD22-K) -> Net-(D1-DP)
- RN6 pad 6: Net-(LD30-K) -> Net-(D1-G)
- RN6 pad 7: Net-(LD27-K) -> Net-(D1-F)
- RN6 pad 8: Net-(LD24-K) -> Net-(D1-E)
- RN7 pad 2: Net-(LD32-K) -> GND
- RN7 pad 3: Net-(LD33-K) -> GND
- RN7 pad 4: Net-(LD34-K) -> GND
- RN7 pad 5: Net-(LD35-K) -> Net-(LD18-K)
- RN7 pad 6: Net-(LD36-K) -> Net-(LD17-K)
- RN7 pad 7: Net-(LD37-K) -> Net-(LD16-K)
- RN7 pad 8: Net-(LD38-K) -> Net-(LD15-K)
- RN8 pad 1: VCC -> GND
- RN8 pad 2: Net-(D30-K) -> GND
- RN8 pad 3: Net-(D2-K) -> GND
- RN8 pad 4: Net-(D6-K) -> GND
- RN8 pad 5: /Address BUS/MEMMode -> Net-(LD22-K)
- RN8 pad 6: /ALU/I0a -> Net-(LD21-K)
- RN8 pad 7: Net-(D18-K) -> Net-(LD20-K)
- RN8 pad 8: Net-(D22-K) -> Net-(LD19-K)
- SW1 pad 1: Net-(IC1-~{CS}) -> Net-(IC5-1A0)
- SW1 pad 2: Net-(J2-Pin_1) -> Net-(IC5-1A1)
- SW1 pad 3: GND -> Net-(IC5-1A2)
- SW2 pad 1: Net-(IC16-OE) -> GND
- SW2 pad 2: unconnected-(SW2-C-Pad2) -> Net-(RN14A-R1.1)
- SW3 pad 2: Net-(R7-Pad2) -> Net-(RN14B-R2.1)
- SW4 pad 1: GND -> Net-(SW4-C)
- SW4 pad 2: Net-(R10-Pad1) -> Net-(SW4-B)
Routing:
- net GND: track 1630.3 -> 0.00 mm, vias 43 -> 0
- net VCC: track 1368.7 -> 0.00 mm, vias 30 -> 0
- net ~{RESET}: track 484.7 -> 0.00 mm, vias 13 -> 0
- net CLK: track 339.2 -> 0.00 mm, vias 7 -> 0
- net /Instruction Decoder/Carry_Flg: track 302.1 -> 0.00 mm, vias 10 -> 0
- net /Address BUS/Instruction_0: track 301.0 -> 0.00 mm, vias 12 -> 0
- net /Address BUS/Instruction_7: track 300.9 -> 0.00 mm, vias 12 -> 0
- net /ALU/ALU_in_B3: track 286.8 -> 0.00 mm, vias 13 -> 0
- net /Data BUS/Stack2: track 274.4 -> 0.00 mm, vias 15 -> 0
- net /ALU/ALU_in_A0: track 259.8 -> 0.00 mm, vias 10 -> 0
- net /ALU/I2a: track 257.7 -> 0.00 mm, vias 7 -> 0
- net /Instruction Decoder/ALU_~{Eb}: track 256.3 -> 0.00 mm, vias 9 -> 0
- net /Data BUS/Stack1: track 252.9 -> 0.00 mm, vias 12 -> 0
- net /ALU/I3a: track 251.3 -> 0.00 mm, vias 7 -> 0
- net /Data BUS/Stack3: track 241.8 -> 0.00 mm, vias 10 -> 0
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- removed copper zone on B.Cu, net GND
- removed copper zone on F.Cu, net GND
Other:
- board size 150.4 x 175 mm -> 100 x 100 mm
- board text removed: "A0"
- board text removed: "A7"
- board text removed: "ALU"
- board text removed: "Address Bus"
- board text removed: "CARRY"
- board text removed: "CLOCK"
- board text removed: "Clock and Reset"
- board text removed: "D0"
- board text removed: "Data Bus"
- board text removed: "Data Bus Control"
- board text removed: "Designed and assenbled in Japan 2509 DGK"
- board text removed: "Expantion Connector"
- board text removed: "HC4_CPU Rev 1.2"
- board text removed: "Instruction decoder"
- board text removed: "LSB"
- board text removed: "Level_A"
- board text removed: "Level_B"
- board text removed: "Level_C"
- board text removed: "MSB"
- board text removed: "PC"
- board text removed: "PC0"
- board text removed: "PC11"
- board text removed: "POWER"
- board text removed: "Program Counter"
- board text removed: "RESET"
- board text removed: "Stack Unit"
- board text removed: "ZERO"

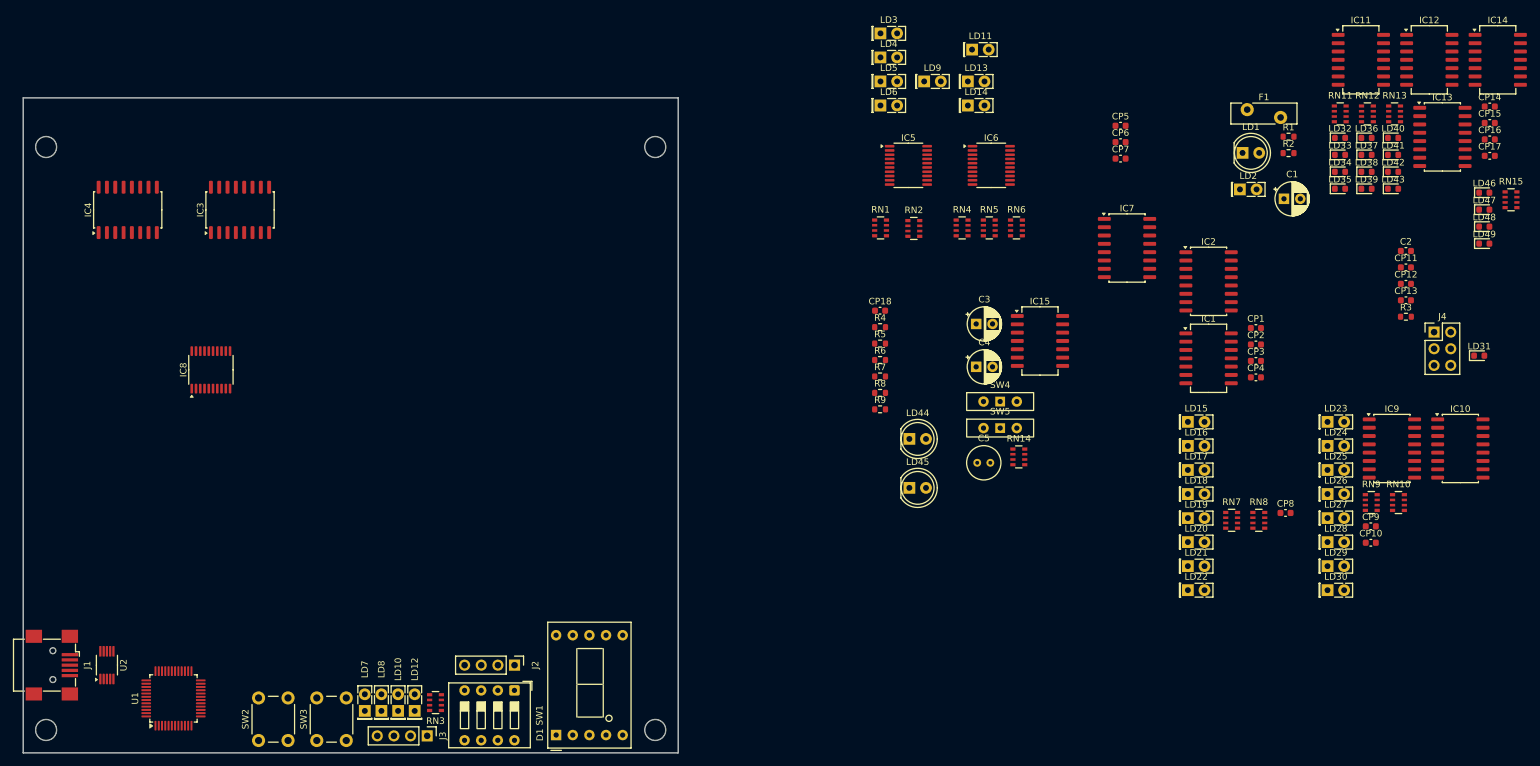
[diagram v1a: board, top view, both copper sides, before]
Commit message: 配線進捗、7474を使った変な回路
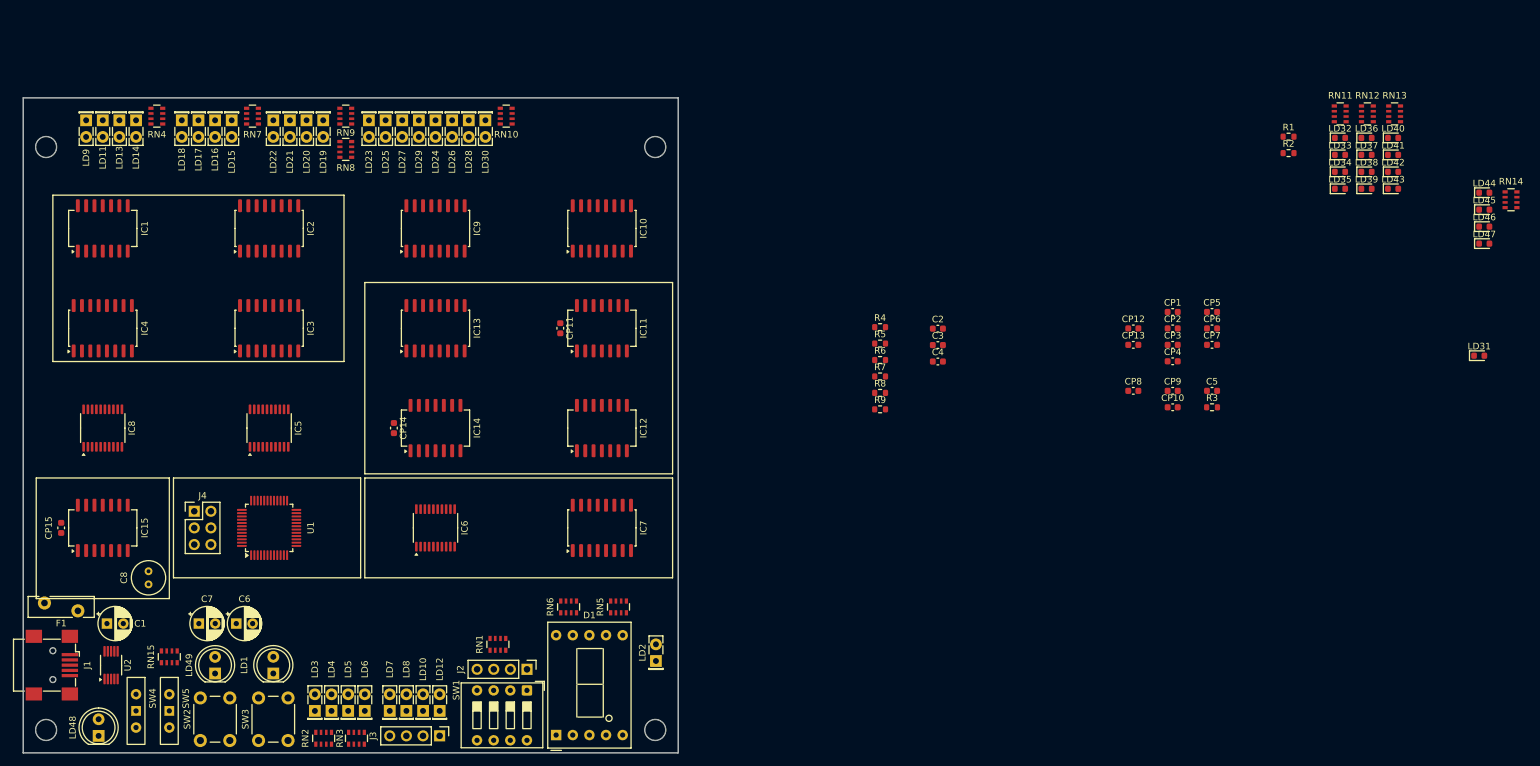
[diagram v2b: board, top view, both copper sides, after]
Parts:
- removed the CP15 at (268.9, 58.8)
- removed CP16, CP17: 0.1u, Capacitor_SMD:C_0603_1608Metric
- added C3: 0.1u, Capacitor_SMD:C_0603_1608Metric, F.Cu at (184.6, 92.7)
- added C4: 0.1u, Capacitor_SMD:C_0603_1608Metric, F.Cu at (184.6, 95.2)
- added C5: 0.1u, Capacitor_SMD:C_0603_1608Metric, F.Cu at (226.5, 99.7)
- moved F1 194.2 mm to (53.4, 133.3), turned to 180 degrees
- moved J4 191.3 mm to (71.1, 118.1)
- moved C1 191.0 mm to (57.8, 135.3)
- moved CP14 174.4 mm to (101.6, 105.4), turned to -90 degrees
- moved IC1 170.0 mm to (57.1, 74.9), turned to 90 degrees
- moved LD1 168.0 mm to (83.2, 142.9), turned to 90 degrees
- moved RN9 167.3 mm to (94.2, 57.8)
- moved LD18 163.9 mm to (69.2, 58.4), turned to -90 degrees
- moved RN7 161.7 mm to (80.0, 57.8), turned to 180 degrees
- moved LD17 160.2 mm to (71.8, 58.4), turned to -90 degrees
- moved LD22 157.0 mm to (83.2, 58.4), turned to -90 degrees
- moved LD16 156.6 mm to (74.3, 58.4), turned to -90 degrees
- moved IC13 156.5 mm to (108.0, 90.2), turned to 90 degrees
- moved LD29 154.5 mm to (105.4, 58.4), turned to -90 degrees
- moved LD27 153.8 mm to (102.9, 58.4), turned to -90 degrees
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- renumbered C3 to C6, C4 to C7, C5 to C8, CP18 to CP15, IC14 to IC11, IC11 to IC14, LD46 to LD44, LD47 to LD45, LD48 to LD46, LD49 to LD47, LD44 to LD48, LD45 to LD49, RN15 to RN14, RN14 to RN15
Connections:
- C2 pad 1: GND -> VCC
- C2 pad 2: Net-(U2-V3) -> GND
- IC11 pad 10: VCC -> Net-(IC11B-~{S})
- IC11 pad 13: VCC -> GND
- IC11 pad 9: unconnected-(IC14B-Q-Pad9) -> Net-(IC11B-Q)
- IC13 pad 15: Net-(IC13-Y) -> Net-(IC11B-~{S})
- IC13 pad 2: /ALU/Instruction_0 -> VCC
- IC13 pad 3: VCC -> Net-(IC11B-~{S})
- IC13 pad 4: /Instruction Decoder/~{JMP} -> Net-(IC13-Z)
- IC13 pad 5: Net-(IC13-Y) -> Net-(IC11B-Q)
- IC13 pad 9: /Instruction Decoder/~{Is_JP} -> /ALU/Instruction_0
- IC14 pad 1: /Instruction Decoder/READ -> Net-(IC14-Pad1)
- IC14 pad 11: VCC -> /ALU/Instruction_6
- IC14 pad 12: VCC -> /ALU/Instruction_5
- IC14 pad 13: unconnected-(IC11-Pad13) -> /Instruction Decoder/READ
- IC14 pad 2: /ALU/Instruction_6 -> Net-(IC13-Z)
- IC14 pad 3: /ALU/Instruction_5 -> /Instruction Decoder/~{Is_JP}
- IC14 pad 4: unconnected-(IC11-Pad4) -> /Instruction Decoder/~{JMP}
- IC14 pad 5: VCC -> Net-(IC14-Pad1)
- IC14 pad 6: VCC -> Net-(IC14-Pad1)
- IC6 pad 13: /ALU/ALU_OUT0 -> /ALU/ALU_OUT3
- IC6 pad 14: /ALU/ALU_OUT1 -> /ALU/ALU_OUT2
- IC6 pad 17: /ALU/ALU_OUT2 -> /ALU/ALU_OUT1
- IC6 pad 18: /ALU/ALU_OUT3 -> /ALU/ALU_OUT0
- LD10 pad 2: Net-(IC6-Q5) -> Net-(IC6-Q6)
- LD12 pad 2: Net-(IC6-Q4) -> Net-(IC6-Q7)
- LD48 pad 2: Net-(RN14C-R3.1) -> Net-(RN15A-R1.1)
- LD7 pad 2: Net-(IC6-Q7) -> Net-(IC6-Q4)
- LD8 pad 2: Net-(IC6-Q6) -> Net-(IC6-Q5)
- R4 pad 1: Net-(RN14A-R1.1) -> Net-(RN15B-R2.1)
- R5 pad 1: Net-(RN14B-R2.1) -> Net-(RN15C-R3.1)
- RN15 pad 1: Net-(RN14A-R1.1) -> Net-(RN15A-R1.1)
- RN15 pad 2: Net-(RN14B-R2.1) -> Net-(RN15B-R2.1)
- RN15 pad 3: Net-(RN14C-R3.1) -> Net-(RN15C-R3.1)
- RN3 pad 5: Net-(LD7-K) -> Net-(LD12-K)
- RN3 pad 6: Net-(LD8-K) -> Net-(LD10-K)
- RN3 pad 7: Net-(LD10-K) -> Net-(LD8-K)
- RN3 pad 8: Net-(LD12-K) -> Net-(LD7-K)
- RN8 pad 5: Net-(LD22-K) -> Net-(LD19-K)
- RN8 pad 6: Net-(LD21-K) -> Net-(LD20-K)
- RN8 pad 7: Net-(LD20-K) -> Net-(LD21-K)
- RN8 pad 8: Net-(LD19-K) -> Net-(LD22-K)
- RN9 pad 5: Net-(LD29-K) -> Net-(LD23-K)
- RN9 pad 6: Net-(LD27-K) -> Net-(LD25-K)
- RN9 pad 7: Net-(LD25-K) -> Net-(LD27-K)
- RN9 pad 8: Net-(LD23-K) -> Net-(LD29-K)
- SW2 pad 2: Net-(RN14A-R1.1) -> Net-(RN15B-R2.1)
- SW3 pad 2: Net-(RN14B-R2.1) -> Net-(RN15C-R3.1)
- SW4 pad 1: Net-(SW4-C) -> Net-(SW4-B)
- SW4 pad 2: Net-(SW4-B) -> Net-(SW4-C)

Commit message: もち
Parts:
- removed the LD44 at (268.1, 69.5)
- removed the LD45 at (268.1, 72.1)
- moved LD31 202.7 mm to (69.2, 137.2)
- moved C5 175.1 mm to (55.9, 139.1), turned to 90 degrees
- moved R1 170.8 mm to (87.6, 141.6), turned to 90 degrees
- moved CP1 170.2 mm to (50.8, 74.9), turned to -90 degrees
- moved CP4 169.8 mm to (50.8, 90.2), turned to -90 degrees
- moved RN12 169.5 mm to (85.7, 98.4)
- moved LD39 164.8 mm to (89.5, 106.0), turned to 180 degrees
- moved LD36 164.7 mm to (89.5, 102.9), turned to 180 degrees
- moved LD37 164.5 mm to (89.5, 99.7), turned to 180 degrees
- moved LD38 164.4 mm to (89.5, 96.5), turned to 180 degrees
- moved CP8 161.9 mm to (52.7, 105.4), turned to -90 degrees
- moved R3 160.7 mm to (69.2, 135.3)
- moved CP5 149.5 mm to (78.1, 105.4), turned to -90 degrees
- moved CP2 145.1 mm to (76.2, 74.9), turned to -90 degrees
- moved CP3 144.3 mm to (76.2, 90.2), turned to -90 degrees
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- renumbered LD38 to LD36, LD36 to LD38, LD46 to LD44, LD47 to LD45, LD48 to LD46, LD49 to LD47
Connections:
- LD36 pad 1: Net-(LD38-K) -> /Instruction Decoder/~{STACK_LE}
- LD36 pad 2: /Instruction Decoder/~{STACK_LE} -> Net-(RN12C-R3.2)
- LD37 pad 1: Net-(LD37-K) -> /Instruction Decoder/~{RAM_RD}
- LD37 pad 2: /Instruction Decoder/~{RAM_RD} -> Net-(RN12B-R2.2)
- LD38 pad 1: Net-(LD36-K) -> /Instruction Decoder/~{RAM_WR}
- LD38 pad 2: /Instruction Decoder/~{RAM_WR} -> Net-(RN12A-R1.2)
- RN11 pad 5: Net-(LD35-K) -> Net-(LD32-K)
- RN11 pad 6: Net-(LD34-K) -> Net-(LD33-K)
- RN11 pad 7: Net-(LD33-K) -> Net-(LD34-K)
- RN11 pad 8: Net-(LD32-K) -> Net-(LD35-K)
- RN12 pad 1: GND -> VCC
- RN12 pad 2: GND -> VCC
- RN12 pad 3: GND -> VCC
- RN12 pad 6: Net-(LD38-K) -> Net-(RN12C-R3.2)
- RN12 pad 7: Net-(LD37-K) -> Net-(RN12B-R2.2)
- RN12 pad 8: Net-(LD36-K) -> Net-(RN12A-R1.2)
- RN14 pad 7: Net-(LD45-K) (its old number) -> unconnected-(RN14-R2.2-Pad7)
- RN14 pad 8: Net-(LD44-K) (its old number) -> unconnected-(RN14-R1.2-Pad8)
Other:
- board text added: "JP命令ではない"
- board text added: "ジャンプしない"
- board text added: "スタック 有効"
- board text added: "フラグ有効"
- board text added: "レジスタ 書き込み"
- board text added: "レジスタ 読み取り"
- board text added: "レジスタ読む"
- board text added: "繰り上がり"

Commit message: 自動配線前バックアップ
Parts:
- moved RN14 157.4 mm to (119.4, 108.6), turned to 90 degrees
- moved LD44 152.7 mm to (118.1, 104.1), turned to 90 degrees
- moved LD45 149.1 mm to (121.3, 104.1), turned to 90 degrees
- moved R6 121.9 mm to (59.1, 130.2)
- moved R7 120.7 mm to (59.1, 128.3)
- moved R9 119.3 mm to (57.1, 114.9)
- moved R8 113.7 mm to (66.0, 129.5), turned to 90 degrees
- moved RN13 8.64 mm to (126.4, 96.5), turned to 180 degrees
- moved LD41 4.02 mm to (118.6, 93.3)
- moved LD40 4.02 mm to (116.1, 93.3)
- moved LD42 4.02 mm to (121.2, 93.3)
- moved LD43 4.02 mm to (123.8, 93.3)

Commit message: 基板完成
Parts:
- moved C5 4.10 mm to (57.4, 135.3), turned to -90 degrees
- moved C3 0.63 mm to (83.8, 114.3), turned to 180 degrees
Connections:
- RN10 pad 5: Net-(LD30-K) -> Net-(LD24-K)
- RN10 pad 6: Net-(LD28-K) -> Net-(LD26-K)
- RN10 pad 7: Net-(LD26-K) -> Net-(LD28-K)
- RN10 pad 8: Net-(LD24-K) -> Net-(LD30-K)
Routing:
- net GND: track 0.00 -> 888.7 mm, vias 0 -> 104
- net VCC: track 0.00 -> 744.1 mm, vias 0 -> 12
- net CLK: track 0.00 -> 223.3 mm, vias 0 -> 7
- net /ALU/Instruction_1: track 0.00 -> 213.8 mm, vias 0 -> 7
- net /Instruction Decoder/READ: track 0.00 -> 191.9 mm, vias 0 -> 7
- net /ALU/ALU_OUT1: track 0.00 -> 190.7 mm, vias 0 -> 9
- net /ALU/ALU_in_A3: track 0.00 -> 185.2 mm, vias 0 -> 5
- net /ALU/ALU_in_A0: track 0.00 -> 172.8 mm, vias 0 -> 7
- net /ALU/ALU_in_A2: track 0.00 -> 164.0 mm, vias 0 -> 5
- net /ALU/ALU_OUT2: track 0.00 -> 160.7 mm, vias 0 -> 12
- net /ALU/Instruction_0: track 0.00 -> 158.6 mm, vias 0 -> 7
- net /ALU/ALU_in_A1: track 0.00 -> 154.5 mm, vias 0 -> 5
- net ~{RESET}: track 0.00 -> 153.6 mm, vias 0 -> 5
- net /ALU/Instruction_6: track 0.00 -> 146.1 mm, vias 0 -> 5
- net /ALU/ALU_OUT0: track 0.00 -> 142.7 mm, vias 0 -> 11
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- added copper zone on B.Cu, net GND
- added copper zone on F.Cu, net GND

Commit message: 振出しに戻る
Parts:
- moved C5 4.10 mm to (55.9, 139.1), turned to 90 degrees
- moved C3 0.63 mm to (83.8, 113.7), turned to 90 degrees
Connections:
- IC6 pad 13: /ALU/ALU_OUT3 -> /ALU/ALU_OUT0
- IC6 pad 14: /ALU/ALU_OUT2 -> /ALU/ALU_OUT1
- IC6 pad 17: /ALU/ALU_OUT1 -> /ALU/ALU_OUT2
- IC6 pad 18: /ALU/ALU_OUT0 -> /ALU/ALU_OUT3
- IC6 pad 3: /ALU/ALU_OUT0 -> /ALU/ALU_OUT3
- IC6 pad 4: /ALU/ALU_OUT1 -> /ALU/ALU_OUT2
- IC6 pad 7: /ALU/ALU_OUT2 -> /ALU/ALU_OUT1
- IC6 pad 8: /ALU/ALU_OUT3 -> /ALU/ALU_OUT0
- IC8 pad 13: /ALU/ALU_in_A0 -> /ALU/ALU_in_A3
- IC8 pad 14: /ALU/ALU_in_A1 -> /ALU/ALU_in_A2
- IC8 pad 17: /ALU/ALU_in_A2 -> /ALU/ALU_in_A1
- IC8 pad 18: /ALU/ALU_in_A3 -> /ALU/ALU_in_A0
- J3 pad 1: Net-(IC6-Q0) -> Net-(IC6-Q3)
- J3 pad 2: Net-(IC6-Q1) -> Net-(IC6-Q2)
- J3 pad 3: Net-(IC6-Q2) -> Net-(IC6-Q1)
- J3 pad 4: Net-(IC6-Q3) -> Net-(IC6-Q0)
- LD10 pad 2: Net-(IC6-Q6) -> Net-(IC6-Q5)
- LD12 pad 2: Net-(IC6-Q7) -> Net-(IC6-Q4)
- LD7 pad 2: Net-(IC6-Q4) -> Net-(IC6-Q7)
- LD8 pad 2: Net-(IC6-Q5) -> Net-(IC6-Q6)
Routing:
- net GND: track 888.7 -> 473.7 mm, vias 104 -> 2
- net VCC: track 744.1 -> 427.8 mm, vias 12 -> 7
- net CLK: track 223.3 -> 0.00 mm, vias 7 -> 0
- net /ALU/Instruction_1: track 213.8 -> 0.00 mm, vias 7 -> 0
- net /Instruction Decoder/READ: track 191.9 -> 0.00 mm, vias 7 -> 0
- net /ALU/ALU_OUT1: track 190.7 -> 0.00 mm, vias 9 -> 0
- net /ALU/ALU_in_A3: track 185.2 -> 0.00 mm, vias 5 -> 0
- net /ALU/ALU_in_A0: track 172.8 -> 0.00 mm, vias 7 -> 0
- net /ALU/ALU_in_A2: track 164.0 -> 0.00 mm, vias 5 -> 0
- net /ALU/ALU_OUT2: track 160.7 -> 0.00 mm, vias 12 -> 0
- net /ALU/Instruction_0: track 158.6 -> 0.00 mm, vias 7 -> 0
- net /ALU/ALU_in_A1: track 154.5 -> 0.00 mm, vias 5 -> 0
- net ~{RESET}: track 153.6 -> 0.00 mm, vias 5 -> 0
- net /ALU/Instruction_6: track 146.1 -> 0.00 mm, vias 5 -> 0
- net /ALU/ALU_OUT0: track 142.7 -> 0.00 mm, vias 11 -> 0
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- removed copper zone on B.Cu, net GND
- removed copper zone on F.Cu, net GND
